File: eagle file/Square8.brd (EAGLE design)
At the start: 49.5 x 53 mm, 29 parts, among them J3 CR2032-172, U1 ATmega328mu, U2 CH340T, U3 CN3065, X1 16MHz, X2 12MHz

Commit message: update eagle file
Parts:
- removed J2: (no value), Connector :JST-SMD-2.0-90D
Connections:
- net COL6 renamed N$82
- net BAT: no longer J2.+
- net GND: no longer J2.-
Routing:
- net BAT: track 105.8 -> 50.2 mm, vias 3 -> 1
- net N$77: track 0.00 -> 3.29 mm
- net N$83: track 0.00 -> 2.75 mm
- net N$85: track 0.00 -> 2.75 mm
- net N$82: track 18.4 -> 20.4 mm
- net ROW1: track 23.3 -> 25.1 mm
- net N$79: track 0.00 -> 1.55 mm
- net N$11: track 1.48 -> 2.94 mm
- net N$78: track 0.00 -> 1.43 mm
- net COL2: track 34.2 -> 35.6 mm
- net N$80: track 0.00 -> 1.38 mm
- net N$81: track 0.00 -> 1.25 mm
- net N$75: track 0.00 -> 1.25 mm
- net N$84: track 0.00 -> 1.23 mm
- net N$76: track 0.00 -> 1.20 mm
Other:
- board text added: "+"
- board text added: "-"

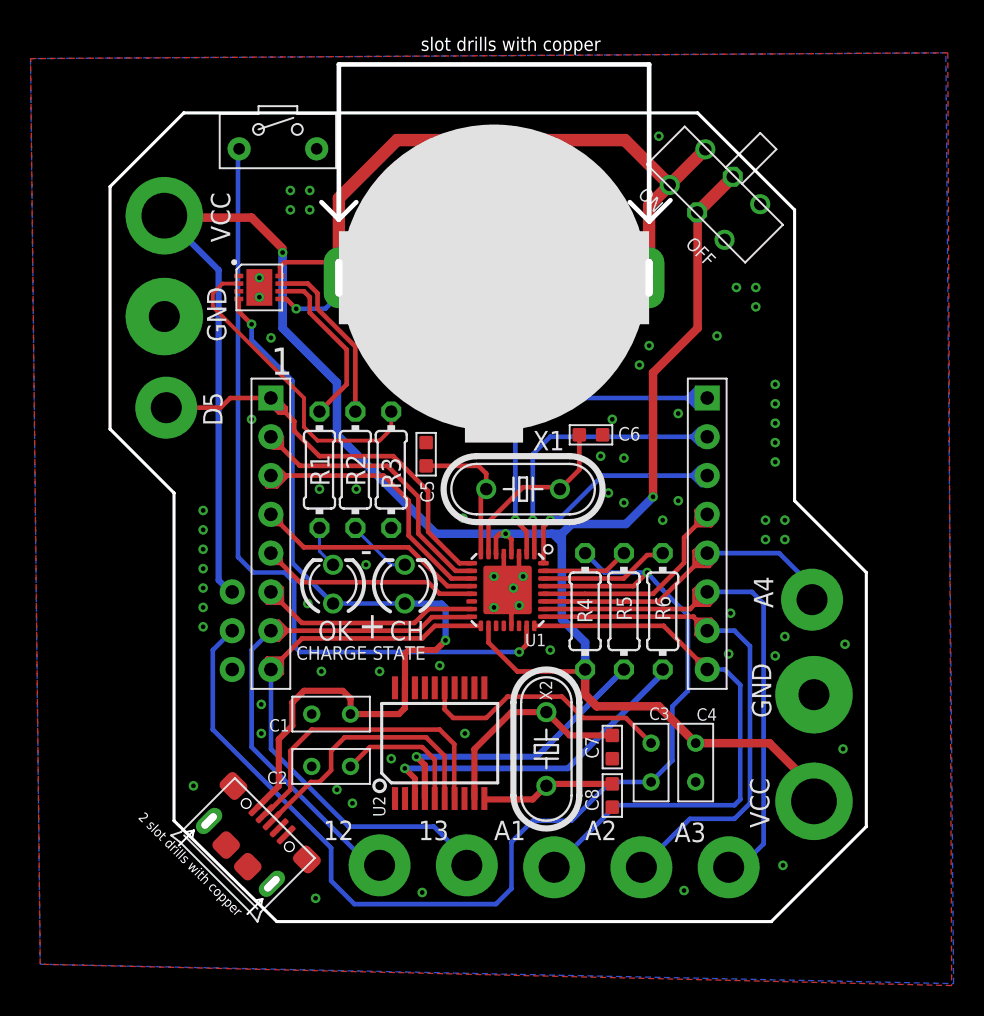
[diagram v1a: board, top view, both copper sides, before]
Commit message: add a pmos, when usb inserted, power will on
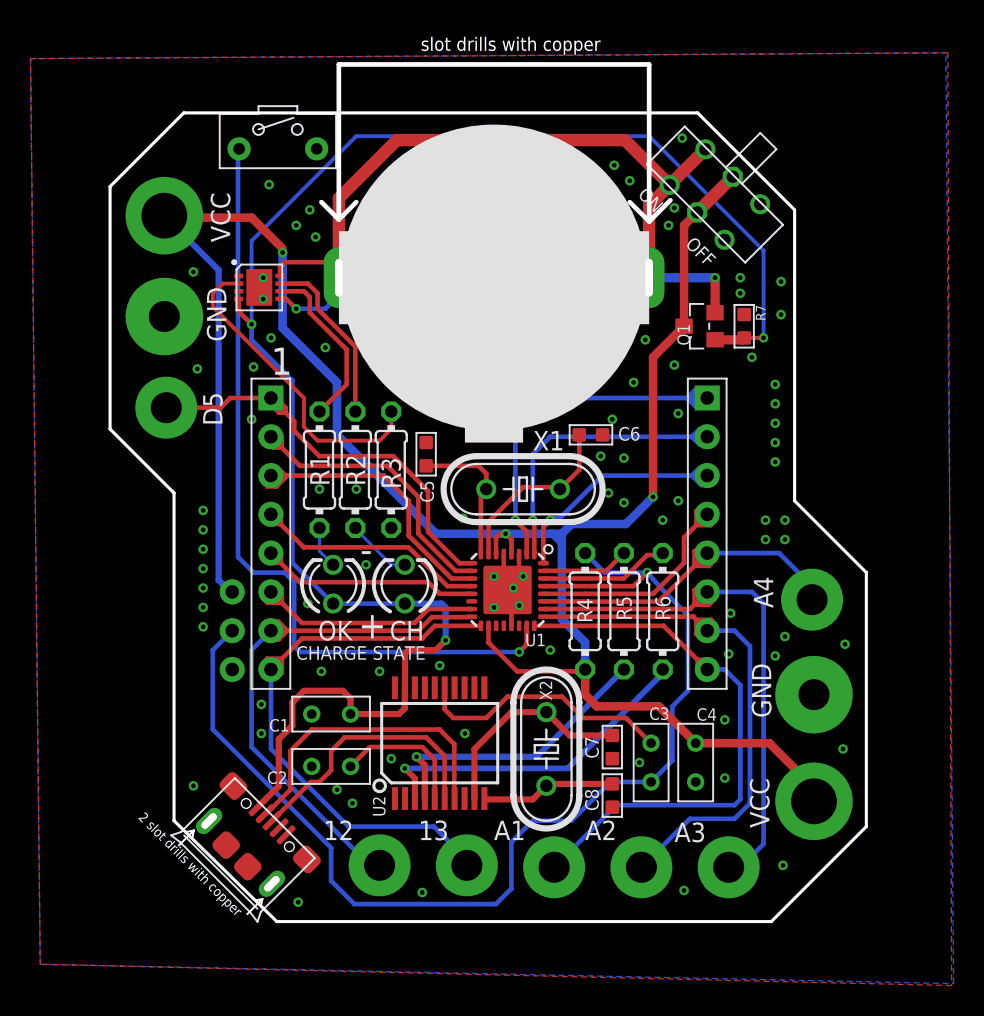
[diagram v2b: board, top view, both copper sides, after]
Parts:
- added Q1: si2305, Discrete:SOT23
- added R7: 100k, Discrete:R0603
- moved U$1 19.3 mm to (31.0, 46.5)
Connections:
- net BAT: now also Q1.2
- net GND: now also R7.1
- net USB5V: now also Q1.1, R7.2
- net VCC: now also Q1.3
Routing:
- net USB5V: track 55.7 -> 109.6 mm, vias 2 -> 3
- net BAT: track 50.2 -> 56.8 mm, vias 1 -> 2
- net GND: vias 73 -> 88
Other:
- board text added: "http://loovee.github.io/Square8/"
- board text removed: "https://github.com/loovee/Square8"

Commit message: improve pcb
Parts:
- added P1: (no value), Discrete:2P-SMD-1.78X1.27
- moved U$1 0.09 mm to (30.9, 46.6)
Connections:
- new net N$86: P1.2, Q1.1, R7.2
- net USB5V: now also P1.1; no longer Q1.1, R7.2
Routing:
- net N$86: track 0.00 -> 6.66 mm, vias 0 -> 1
- net N$4: track 2.78 -> 4.77 mm
- net XTAL1: track 11.9 -> 13.8 mm
- net N$5: track 4.28 -> 5.95 mm
- net N$40: track 8.82 -> 9.99 mm
- net V3: track 8.93 -> 10.1 mm
- net RESET: track 74.3 -> 75.3 mm
- net N$7: track 20.7 -> 21.6 mm
- net PD0/RX: track 8.50 -> 9.40 mm
- net N$3: track 11.3 -> 12.2 mm
- net N$100: track 0.00 -> 0.73 mm
- net XTAL2: track 9.61 -> 10.3 mm
- net N$110: track 0.00 -> 0.70 mm
- net N$111: track 0.00 -> 0.67 mm
- net N$39: track 13.9 -> 14.5 mm
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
